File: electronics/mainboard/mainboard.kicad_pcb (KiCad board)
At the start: 2 copper layers, 40 x 130 mm, 1 part, among them U1 1022

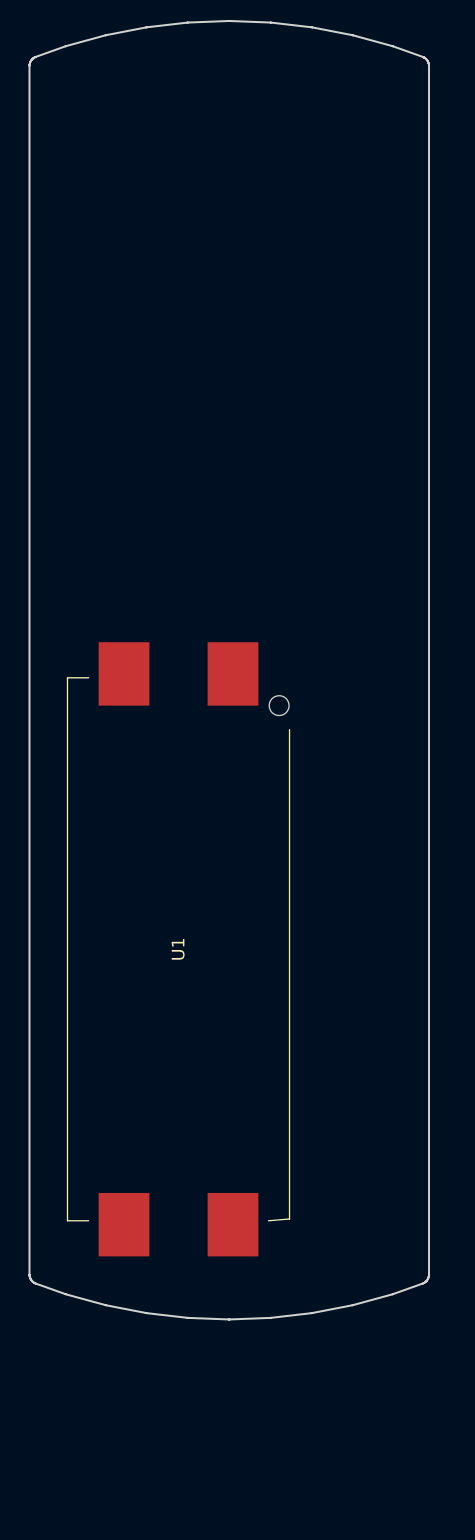
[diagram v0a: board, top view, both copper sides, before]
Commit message: add arduino nano to pcb
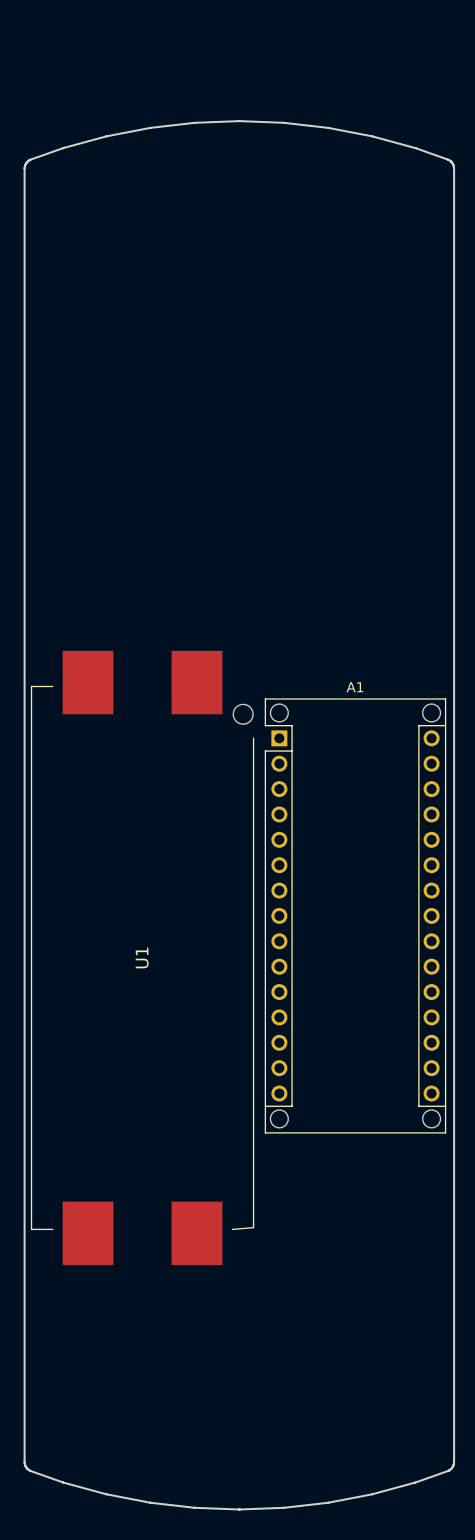
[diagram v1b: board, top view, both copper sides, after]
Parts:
- added A1: Arduino_Nano_v3.x, Module:Arduino_Nano_WithMountingHoles, F.Cu at (114.6, 103.0)
- moved U1 3.70 mm to (100.9, 125.0)
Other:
- board size 40 x 130 mm -> 43 x 139 mm

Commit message: add buttons and ir-led
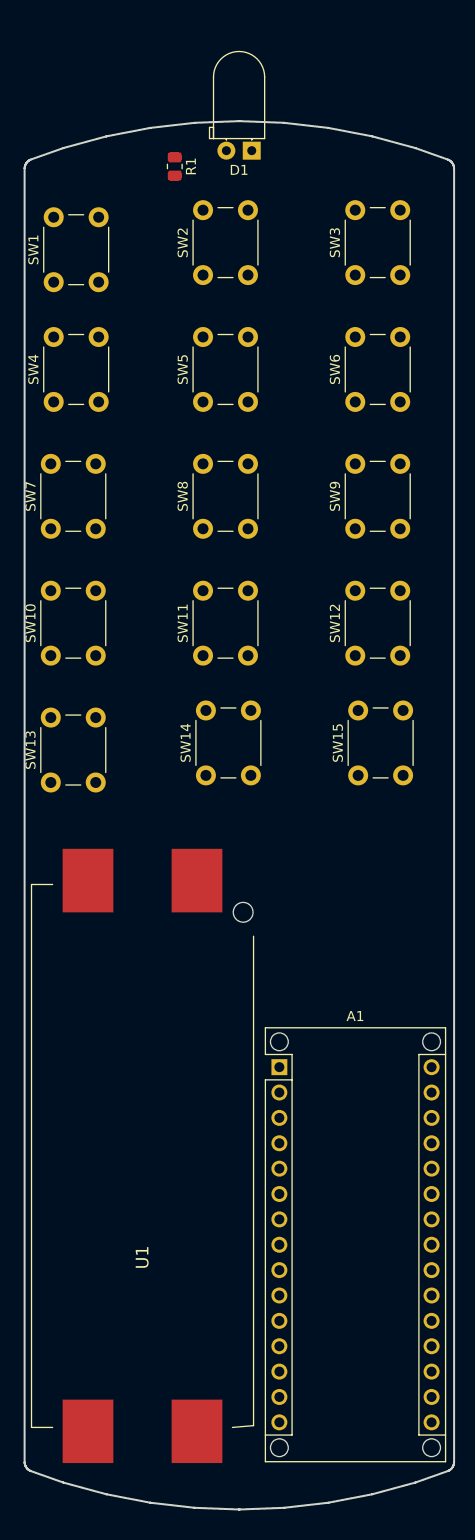
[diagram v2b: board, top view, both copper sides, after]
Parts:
- added D1: LED, LED_THT:LED_D5.0mm_Horizontal_O1.27mm_Z3.0mm, F.Cu at (111.8, 44.1)
- added R1: R, Resistor_SMD:R_0805_2012Metric, F.Cu at (104.1, 45.7)
- added SW1: SW_MEC_5G, Button_Switch_THT:SW_PUSH_6mm, F.Cu at (92.0, 57.3)
- added SW10: SW_MEC_5G, Button_Switch_THT:SW_PUSH_6mm, F.Cu at (91.7, 94.7)
- added SW11: SW_MEC_5G, Button_Switch_THT:SW_PUSH_6mm, F.Cu at (107.0, 94.7)
- added SW12: SW_MEC_5G, Button_Switch_THT:SW_PUSH_6mm, F.Cu at (122.2, 94.7)
- added SW13: SW_MEC_5G, Button_Switch_THT:SW_PUSH_6mm, F.Cu at (91.7, 107.4)
- added SW14: SW_MEC_5G, Button_Switch_THT:SW_PUSH_6mm, F.Cu at (107.3, 106.7)
- added SW15: SW_MEC_5G, Button_Switch_THT:SW_PUSH_6mm, F.Cu at (122.5, 106.7)
- added SW2: SW_MEC_5G, Button_Switch_THT:SW_PUSH_6mm, F.Cu at (107.0, 56.6)
- added SW3: SW_MEC_5G, Button_Switch_THT:SW_PUSH_6mm, F.Cu at (122.2, 56.6)
- added SW4: SW_MEC_5G, Button_Switch_THT:SW_PUSH_6mm, F.Cu at (92.0, 69.3)
- added SW5: SW_MEC_5G, Button_Switch_THT:SW_PUSH_6mm, F.Cu at (107.0, 69.3)
- added SW6: SW_MEC_5G, Button_Switch_THT:SW_PUSH_6mm, F.Cu at (122.2, 69.3)
- added SW7: SW_MEC_5G, Button_Switch_THT:SW_PUSH_6mm, F.Cu at (91.7, 82.0)
- added SW8: SW_MEC_5G, Button_Switch_THT:SW_PUSH_6mm, F.Cu at (107.0, 82.0)
- added SW9: SW_MEC_5G, Button_Switch_THT:SW_PUSH_6mm, F.Cu at (122.2, 82.0)
- moved A1 32.9 mm to (114.6, 135.9)
- moved U1 19.8 mm to (100.9, 144.8)

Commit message: add schematic connections
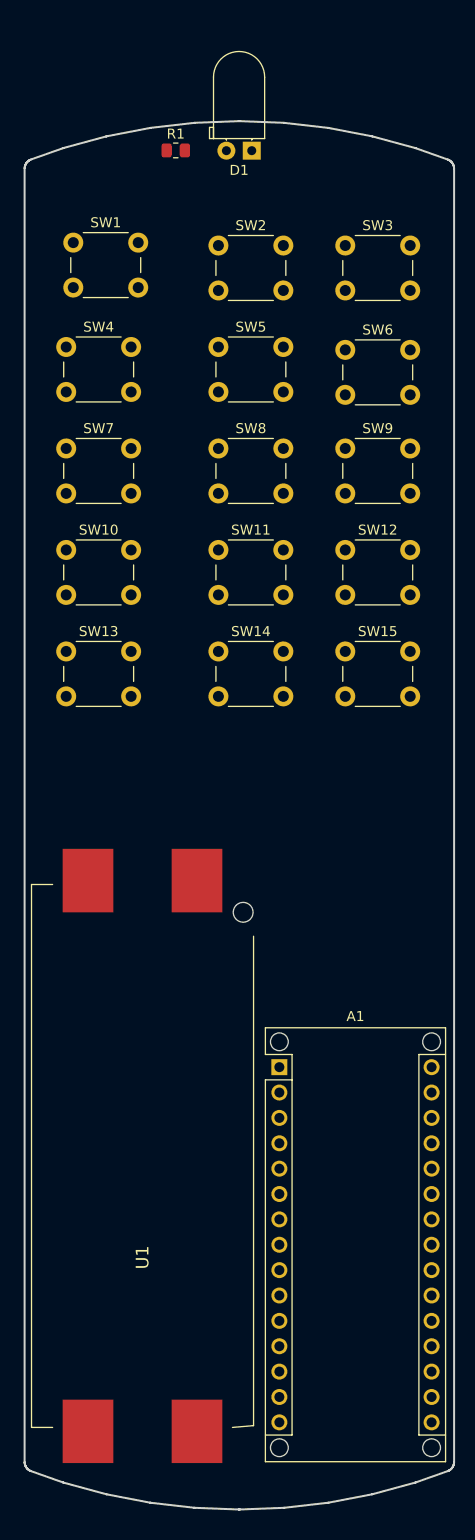
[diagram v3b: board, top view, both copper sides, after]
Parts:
- SW1, SW10, SW11, SW12, SW13, SW14, SW15, SW2, SW3, SW4, SW5, SW6, SW7, SW8, SW9: value SW_MEC_5G -> SW_Push
- moved SW13 13.2 mm to (93.3, 94.3), turned to 0 degrees
- moved SW15 12.5 mm to (121.2, 94.3), turned to 0 degrees
- moved SW14 12.5 mm to (108.5, 94.3), turned to 0 degrees
- moved SW11 10.7 mm to (108.5, 84.1), turned to 0 degrees
- moved SW10 10.7 mm to (93.3, 84.1), turned to 0 degrees
- moved SW12 10.6 mm to (121.2, 84.1), turned to 0 degrees
- moved SW8 8.19 mm to (108.5, 74.0), turned to 0 degrees
- moved SW7 8.19 mm to (93.3, 74.0), turned to 0 degrees
- moved SW9 8.10 mm to (121.2, 74.0), turned to 0 degrees
- moved SW5 5.71 mm to (108.5, 63.8), turned to 0 degrees
- moved SW4 5.64 mm to (93.3, 63.8), turned to 0 degrees
- moved SW6 5.31 mm to (121.2, 64.1), turned to 0 degrees
- moved SW1 4.42 mm to (94.0, 53.3), turned to 0 degrees
- moved SW2 3.34 mm to (108.5, 53.6), turned to 0 degrees
- moved SW3 3.12 mm to (121.2, 53.6), turned to 0 degrees
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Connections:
- A1 pad 1: unconnected-(A1-Pad1) -> /SW2
- A1 pad 10: unconnected-(A1-Pad10) -> /SW8
- A1 pad 11: unconnected-(A1-Pad11) -> /SW9
- A1 pad 12: unconnected-(A1-Pad12) -> /SW10
- A1 pad 13: unconnected-(A1-Pad13) -> /SW11
- A1 pad 14: unconnected-(A1-Pad14) -> /SW12
- A1 pad 15: unconnected-(A1-Pad15) -> /SW13
- A1 pad 16: unconnected-(A1-Pad16) -> /SW14
- A1 pad 17: unconnected-(A1-Pad17) -> +3V0
- A1 pad 19: unconnected-(A1-Pad19) -> Net-(A1-Pad19)
- A1 pad 2: unconnected-(A1-Pad2) -> /SW1
- A1 pad 26: unconnected-(A1-Pad26) -> /SW15
- A1 pad 29: unconnected-(A1-Pad29) -> GND
- A1 pad 4: unconnected-(A1-Pad4) -> GND
- A1 pad 5: unconnected-(A1-Pad5) -> /SW3
- A1 pad 6: unconnected-(A1-Pad6) -> /SW4
- A1 pad 7: unconnected-(A1-Pad7) -> /SW5
- A1 pad 8: unconnected-(A1-Pad8) -> /SW6
- A1 pad 9: unconnected-(A1-Pad9) -> /SW7
- D1 pad 1: unconnected-(D1-Pad1) -> GND
- R1 pad 1: Net-(D1-Pad2) -> Net-(A1-Pad19)
- R1 pad 2: unconnected-(R1-Pad2) -> Net-(D1-Pad2)
- SW1 pad 1: Net-(SW1-Pad1) -> GND
- SW1 pad 2: Net-(SW1-Pad1) -> /SW1
- SW10 pad 1: Net-(SW10-Pad1) -> GND
- SW10 pad 2: Net-(SW10-Pad1) -> /SW12
- SW11 pad 1: Net-(SW11-Pad1) -> GND
- SW11 pad 2: Net-(SW11-Pad1) -> /SW11
- SW12 pad 1: Net-(SW12-Pad1) -> GND
- SW12 pad 2: Net-(SW12-Pad1) -> /SW10
- SW13 pad 1: Net-(SW13-Pad1) -> GND
- SW13 pad 2: Net-(SW13-Pad1) -> /SW15
- SW14 pad 1: Net-(SW14-Pad1) -> GND
- SW14 pad 2: Net-(SW14-Pad1) -> /SW14
- SW15 pad 1: Net-(SW15-Pad1) -> GND
- SW15 pad 2: Net-(SW15-Pad1) -> /SW13
- SW2 pad 1: Net-(SW2-Pad1) -> GND
- SW2 pad 2: Net-(SW2-Pad1) -> /SW3
- SW3 pad 1: Net-(SW3-Pad1) -> GND
- SW3 pad 2: Net-(SW3-Pad1) -> /SW2
- SW4 pad 1: Net-(SW4-Pad1) -> GND
- SW4 pad 2: Net-(SW4-Pad1) -> /SW6
- SW5 pad 1: Net-(SW5-Pad1) -> GND
- SW5 pad 2: Net-(SW5-Pad1) -> /SW5
- SW6 pad 1: Net-(SW6-Pad1) -> GND
- SW6 pad 2: Net-(SW6-Pad1) -> /SW4
- SW7 pad 1: Net-(SW7-Pad1) -> GND
- SW7 pad 2: Net-(SW7-Pad1) -> /SW9
- SW8 pad 1: Net-(SW8-Pad1) -> GND
- SW8 pad 2: Net-(SW8-Pad1) -> /SW8
- SW9 pad 1: Net-(SW9-Pad1) -> GND
- SW9 pad 2: Net-(SW9-Pad1) -> /SW7
- U1 pad 1: unconnected-(U1-Pad1) -> GND
- U1 pad 2: unconnected-(U1-Pad2) -> +3V0
- U1 pad 3: unconnected-(U1-Pad3) -> Net-(U1-Pad3)
- U1 pad 4: unconnected-(U1-Pad4) -> Net-(U1-Pad3)

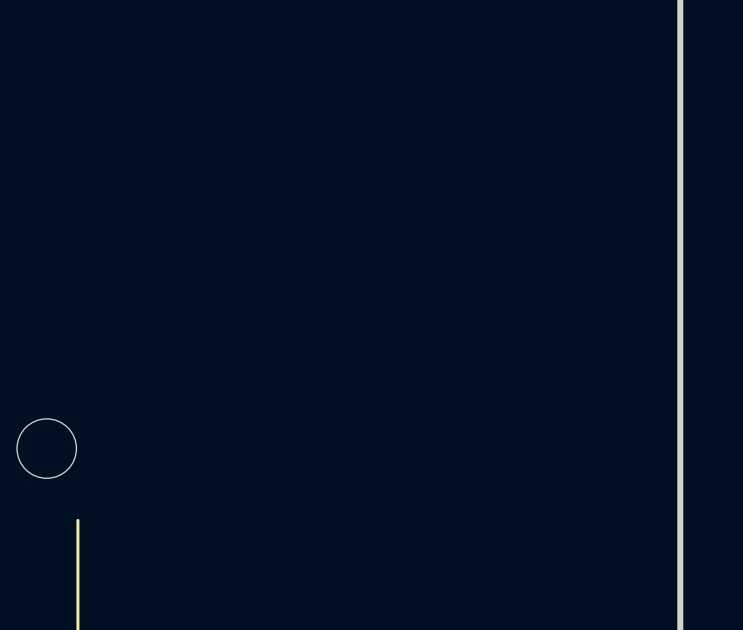
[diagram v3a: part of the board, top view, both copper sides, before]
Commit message: add polarity protection
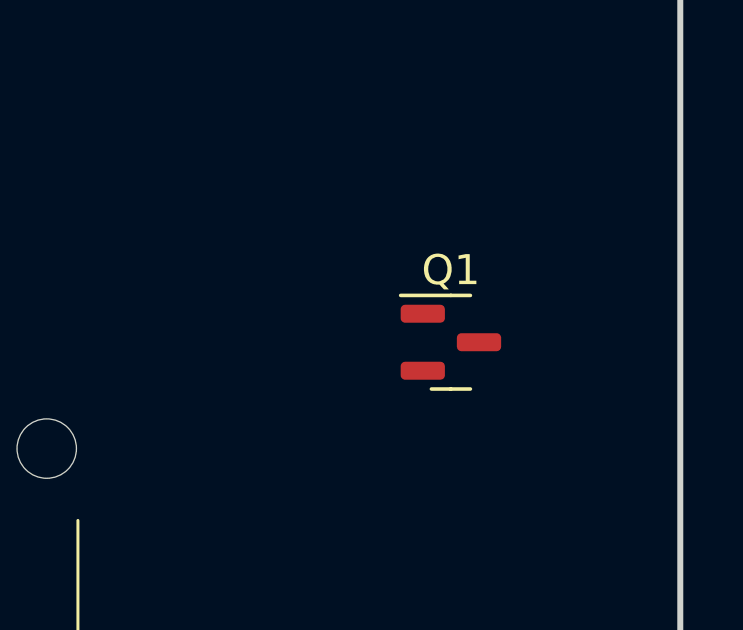
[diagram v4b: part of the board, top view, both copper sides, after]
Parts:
- added Q1: DMN2020LSN-7, Package_TO_SOT_SMD:SOT-23, F.Cu at (124.5, 116.8)
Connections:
- U1 pad 1: GND -> Net-(U1-Pad1)
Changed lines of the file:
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@@
   (net 30 "Net-(U1-Pad3)")
   (net 31 "Net-(A1-Pad19)")
+  (net 32 "Net-(U1-Pad1)")
   (footprint "Button_Switch_THT:SW_PUSH_6mm" (layer "F.Cu")
     (at 121.21 94.27)
@@
     (pad "" np_thru_hole circle locked (at -24.395 -10.075 270) (size 1.98 1.98) (drill 1.98) (layers *.Cu *.Mask))
     (pad "1" smd rect locked (at -27.57 -5.455) (size 5.08 6.35) (layers "F.Cu" "F.Paste" "F.Mask")
-      (net 16 "GND") (pinfunction "1") (pintype "passive"))
+      (net 32 "Net-(U1-Pad1)") (pinfunction "1") (pintype "passive"))
     (pad "2" smd rect locked (at -27.57 5.455) (size 5.08 6.35) (layers "F.Cu" "F.Paste" "F.Mask")
       (net 17 "+3V0") (pinfunction "2") (pintype "passive"))
@@
       (offset (xyz 0 0 0))
       (scale (xyz 1 1 1))
+      (rotate (xyz 0 0 0))
+    )
+  )
+  (footprint "Package_TO_SOT_SMD:SOT-23" (layer "F.Cu")
+    (at 124.46 116.84)
+    (descr "SOT, 3 Pin (https://www.jedec.org/system/files/docs/to-236h.pdf variant AB), generated with kicad-footprint-generator ipc_gullwing_generator.py")
+    (tags "SOT TO_SOT_SMD")
+    (property "Sheetfile" "mainboard.kicad_sch")
+    (property "Sheetname" "")
+    (attr smd)
+    (fp_text reference "Q1" (at 0 -2.4) (layer "F.SilkS")
+      (effects (font (size 1 1) (thickness 0.15)))
+    )
+    (fp_text value "DMN2020LSN-7" (at 0 2.4) (layer "F.Fab")
+      (effects (font (size 1 1) (thickness 0.15)))
+    )
+    (fp_text user "${REFERENCE}" (at 0 0) (layer "F.Fab")
+      (effects (font (size 0.32 0.32) (thickness 0.05)))
+    )
+    (fp_line (start 0 1.56) (end 0.65 1.56) (layer "F.SilkS") (width 0.12))
+    (fp_line (start 0 1.56) (end -0.65 1.56) (layer "F.SilkS") (width 0.12))
+    (fp_line (start 0 -1.56) (end -1.675 -1.56) (layer "F.SilkS") (width 0.12))
+    (fp_line (start 0 -1.56) (end 0.65 -1.56) (layer "F.SilkS") (width 0.12))
+    (fp_line (start -1.92 1.7) (end 1.92 1.7) (layer "F.CrtYd") (width 0.05))
+    (fp_line (start 1.92 -1.7) (end -1.92 -1.7) (layer "F.CrtYd") (width 0.05))
+    (fp_line (start 1.92 1.7) (end 1.92 -1.7) (layer "F.CrtYd") (width 0.05))
+    (fp_line (start -1.92 -1.7) (end -1.92 1.7) (layer "F.CrtYd") (width 0.05))
+    (fp_line (start -0.325 -1.45) (end 0.65 -1.45) (layer "F.Fab") (width 0.1))
+    (fp_line (start 0.65 1.45) (end -0.65 1.45) (layer "F.Fab") (width 0.1))
+    (fp_line (start -0.65 -1.125) (end -0.325 -1.45) (layer "F.Fab") (width 0.1))
+    (fp_line (start -0.65 1.45) (end -0.65 -1.125) (layer "F.Fab") (width 0.1))
+    (fp_line (start 0.65 -1.45) (end 0.65 1.45) (layer "F.Fab") (width 0.1))
+    (pad "1" smd roundrect (at -0.9375 -0.95) (size 1.475 0.6) (layers "F.Cu" "F.Paste" "F.Mask") (roundrect_rratio 0.25)
+      (net 17 "+3V0") (pinfunction "G") (pintype "input"))
+    (pad "2" smd roundrect (at -0.9375 0.95) (size 1.475 0.6) (layers "F.Cu" "F.Paste" "F.Mask") (roundrect_rratio 0.25)
+      (net 16 "GND") (pinfunction "S") (pintype "passive"))
+    (pad "3" smd roundrect (at 0.9375 0) (size 1.475 0.6) (layers "F.Cu" "F.Paste" "F.Mask") (roundrect_rratio 0.25)
+      (net 32 "Net-(U1-Pad1)") (pinfunction "D") (pintype "passive"))
+    (model "${KICAD6_3DMODEL_DIR}/Package_TO_SOT_SMD.3dshapes/SOT-23.wrl"
+      (offset (xyz 0 0 0))
+      (scale (xyz 1 1 1))

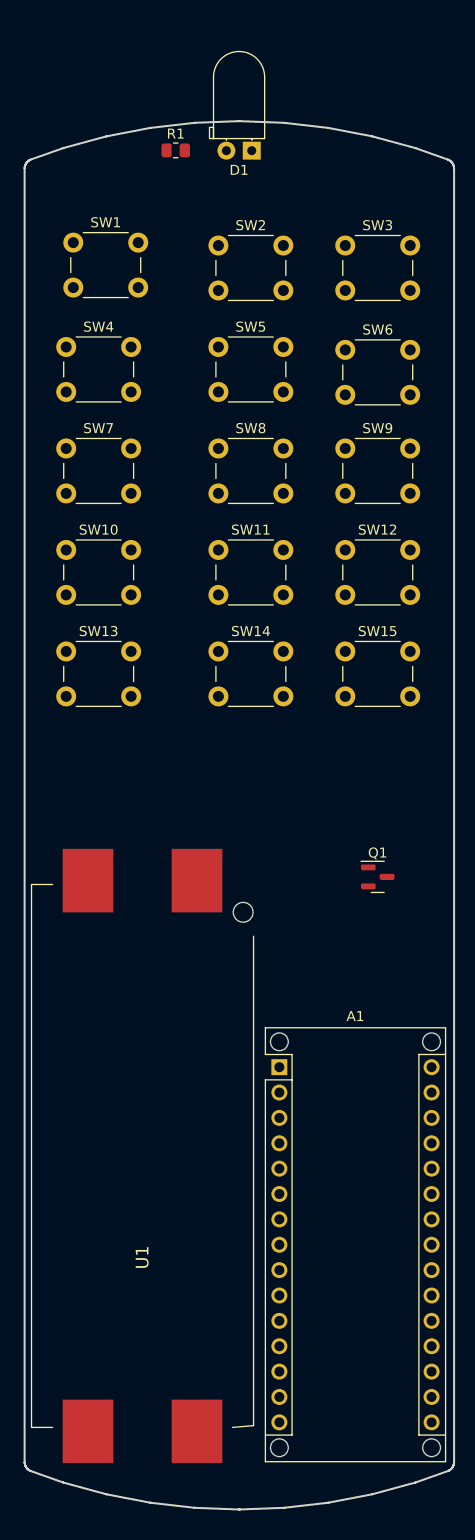
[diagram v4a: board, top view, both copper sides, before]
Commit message: align buttons and ir-led
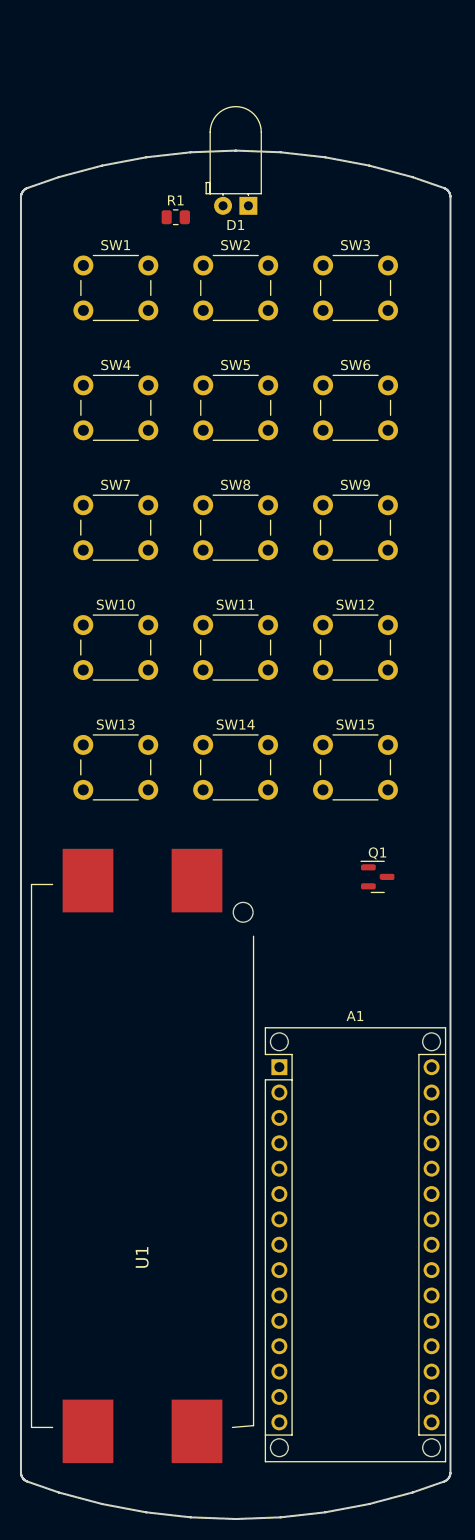
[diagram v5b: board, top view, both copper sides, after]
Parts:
- moved SW15 9.62 mm to (119.0, 103.6)
- moved SW13 9.52 mm to (95.0, 103.6)
- moved SW14 9.48 mm to (107.0, 103.6)
- moved SW12 7.84 mm to (119.0, 91.6)
- moved SW10 7.71 mm to (95.0, 91.6)
- moved SW11 7.67 mm to (107.0, 91.6)
- moved R1 6.69 mm to (104.2, 50.8)
- moved SW9 6.10 mm to (119.0, 79.6)
- moved SW7 5.93 mm to (95.0, 79.6)
- moved SW8 5.88 mm to (107.0, 79.6)
- moved D1 5.53 mm to (111.5, 49.7)
- moved SW4 4.21 mm to (95.0, 67.6)
- moved SW6 4.19 mm to (119.0, 67.6)
- moved SW5 4.13 mm to (107.0, 67.6)
- moved SW3 2.99 mm to (119.0, 55.6)
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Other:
- board size 43 x 139 mm -> 43 x 137 mm
